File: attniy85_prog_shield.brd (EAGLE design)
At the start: 68.6 x 53.3 mm, 2 parts, among them U1 ARDUINOR3-BPLACE

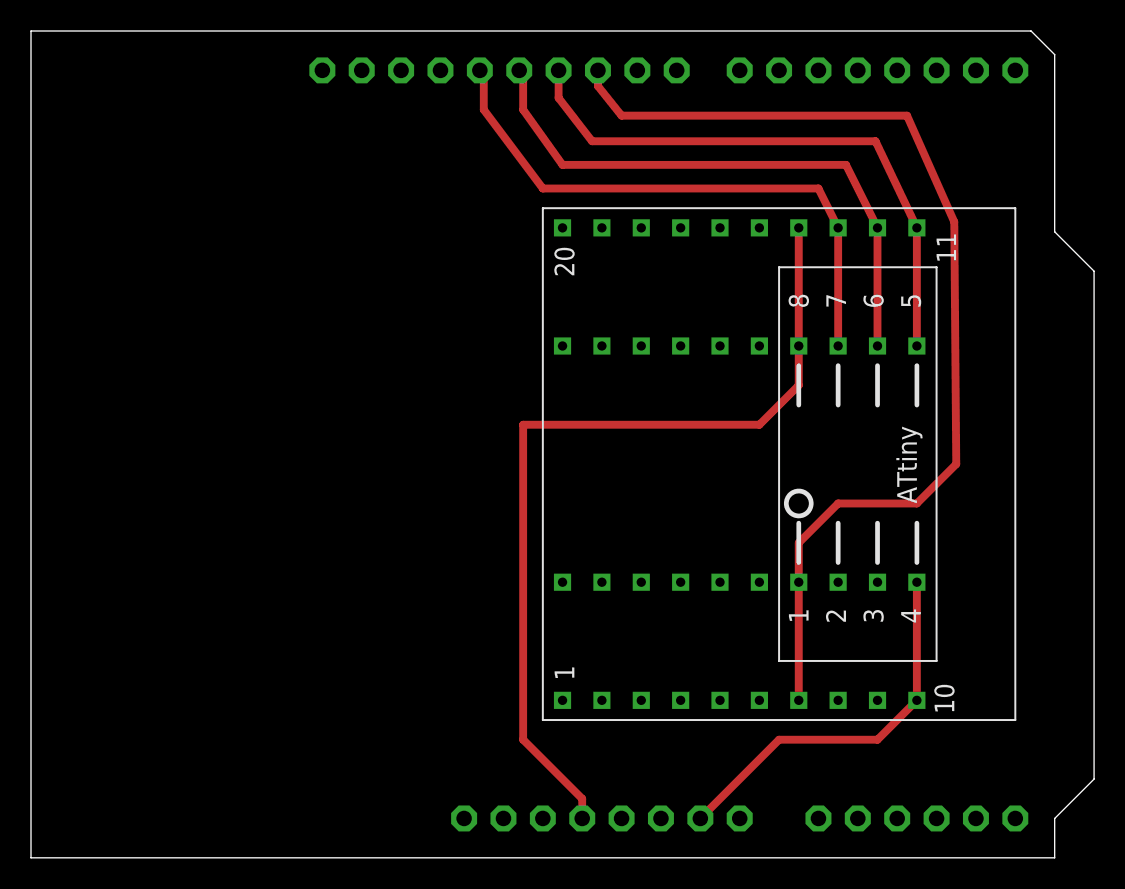
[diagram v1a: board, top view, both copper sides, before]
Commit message: unrouted 2x5pin isp
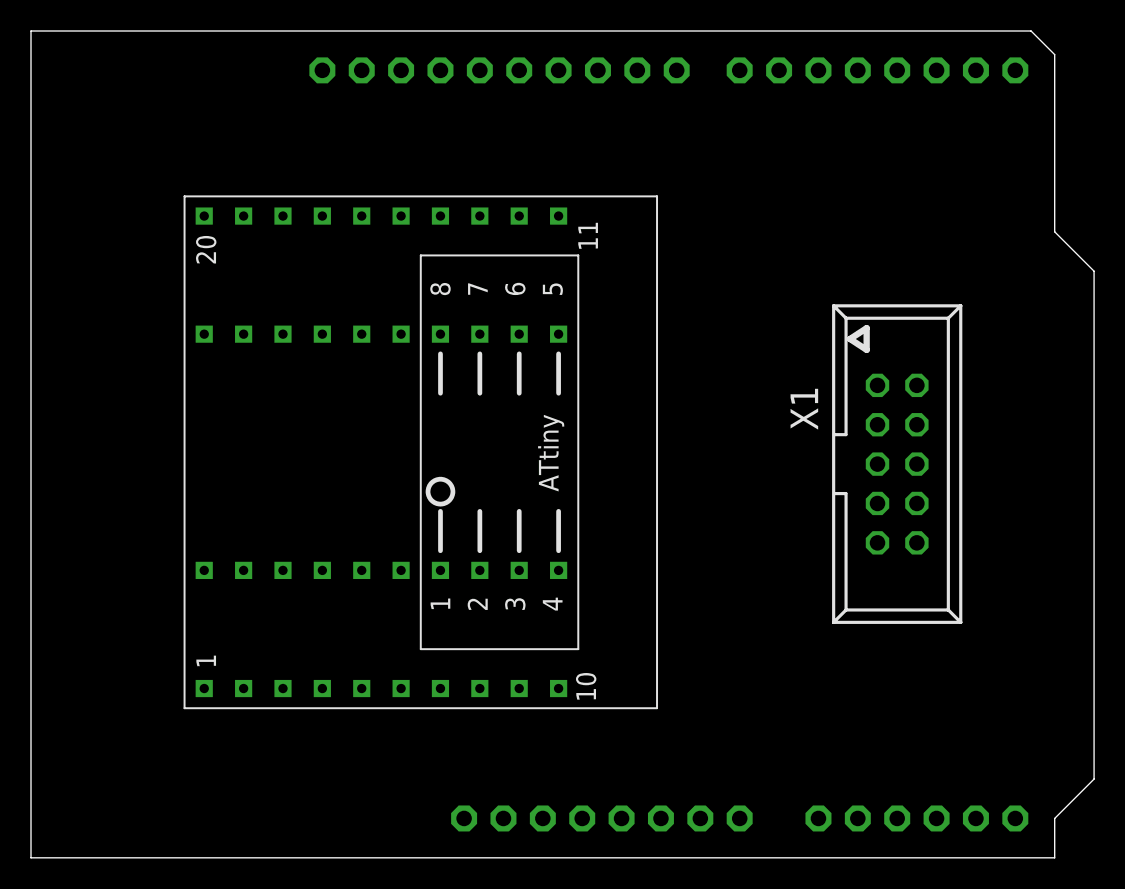
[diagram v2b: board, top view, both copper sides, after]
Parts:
- added X1: ISP10P, attniy85_prog_shield:ISP10PIN
- moved U$1 23.1 mm to (40.4, 9.65)
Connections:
- net GND: now also X1.1
- net MISO: now also X1.2
- net MOSI: now also X1.3
- net RESET: now also X1.4
- net SCK: now also X1.5
- net VCC: now also X1.6
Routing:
- net RESET: track 67.4 -> 0.00 mm
- net VCC: track 56.0 -> 0.00 mm
- net MISO: track 37.5 -> 0.00 mm
- net MOSI: track 37.4 -> 0.00 mm
- net SCK: track 37.2 -> 0.00 mm
- net GND: track 24.7 -> 0.00 mm
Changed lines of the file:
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@@
 <elements>
 <element name="U1" library="ATtami" package="ARDUINOR3-BPLACE" value="ARDUINOR3-BPLACE" x="0" y="0"/>
-<element name="U$1" library="attniy85_prog_shield" package="SOIC8-200MIL" value="SOIC8_200MIL_PROG" x="63.5" y="8.89" rot="R90"/>
+<element name="U$1" library="attniy85_prog_shield" package="SOIC8-200MIL" value="SOIC8_200MIL_PROG" x="40.386" y="9.652" rot="R90"/>
+<element name="X1" library="attniy85_prog_shield" package="ISP10PIN" value="ISP10P" x="55.88" y="25.4" rot="R270"/>
 </elements>
 <signals>
@@
 <contactref element="U1" pad="GND1"/>
 <contactref element="U$1" pad="P$10"/>
-<wire x1="43.18" y1="2.54" x2="48.26" y2="7.62" width="0.508" layer="1"/>
-<wire x1="48.26" y1="7.62" x2="54.61" y2="7.62" width="0.508" layer="1"/>
-<wire x1="54.61" y1="7.62" x2="57.15" y2="10.16" width="0.508" layer="1"/>
 <contactref element="U$1" pad="P$30"/>
-<wire x1="57.15" y1="17.78" x2="57.15" y2="10.16" width="0.508" layer="1"/>
-<wire x1="57.15" y1="17.78" x2="26.416" y2="50.8" width="0" layer="19" extent="1-1"/>
-<wire x1="40.64" y1="2.54" x2="43.18" y2="2.54" width="0" layer="19" extent="1-1"/>
+<contactref element="X1" pad="1"/>
+<wire x1="26.416" y1="50.8" x2="54.61" y2="30.48" width="0" layer="19" extent="1-1"/>
+<wire x1="40.64" y1="2.54" x2="54.61" y2="30.48" width="0" layer="19" extent="1-1"/>
+<wire x1="43.18" y1="2.54" x2="40.64" y2="2.54" width="0" layer="19" extent="1-1"/>
+<wire x1="34.036" y1="10.922" x2="43.18" y2="2.54" width="0" layer="19" extent="1-1"/>
+<wire x1="34.036" y1="18.542" x2="34.036" y2="10.922" width="0" layer="19" extent="1-1"/>
 </signal>
 <signal name="VIN">
@@
 <contactref element="U1" pad="3V"/>
 <contactref element="U$1" pad="P$34"/>
-<wire x1="49.53" y1="40.64" x2="49.53" y2="33.02" width="0.508" layer="1"/>
-<wire x1="49.53" y1="33.02" x2="49.53" y2="30.48" width="0.508" layer="1"/>
-<wire x1="49.53" y1="30.48" x2="46.99" y2="27.94" width="0.508" layer="1"/>
-<wire x1="46.99" y1="27.94" x2="31.75" y2="27.94" width="0.508" layer="1"/>
-<wire x1="31.75" y1="27.94" x2="31.75" y2="7.62" width="0.508" layer="1"/>
-<wire x1="35.56" y1="3.81" x2="35.56" y2="2.54" width="0.508" layer="1"/>
-<wire x1="31.75" y1="7.62" x2="35.56" y2="3.81" width="0.508" layer="1"/>
+<contactref element="X1" pad="6"/>
+<wire x1="26.416" y1="41.402" x2="26.416" y2="33.782" width="0" layer="19" extent="1-1"/>
+<wire x1="57.15" y1="25.4" x2="26.416" y2="33.782" width="0" layer="19" extent="1-1"/>
+<wire x1="35.56" y1="2.54" x2="57.15" y2="25.4" width="0" layer="19" extent="1-1"/>
 </signal>
 <signal name="SCK">
 <contactref element="U1" pad="D13"/>
 <contactref element="U$1" pad="P$13"/>
-<wire x1="28.956" y1="50.8" x2="29.21" y2="50.546" width="0.508" layer="1"/>
-<wire x1="29.21" y1="50.546" x2="29.21" y2="48.26" width="0.508" layer="1"/>
-<wire x1="29.21" y1="48.26" x2="33.02" y2="43.18" width="0.508" layer="1"/>
-<wire x1="33.02" y1="43.18" x2="50.8" y2="43.18" width="0.508" layer="1"/>
-<wire x1="50.8" y1="43.18" x2="52.07" y2="40.64" width="0.508" layer="1"/>
 <contactref element="U$1" pad="P$33"/>
-<wire x1="52.07" y1="40.64" x2="52.07" y2="33.02" width="0.508" layer="1"/>
+<contactref element="X1" pad="5"/>
+<wire x1="28.956" y1="33.782" x2="28.956" y2="41.402" width="0" layer="19" extent="1-1"/>
+<wire x1="28.956" y1="50.8" x2="28.956" y2="41.402" width="0" layer="19" extent="1-1"/>
+<wire x1="54.61" y1="25.4" x2="28.956" y2="50.8" width="0" layer="19" extent="1-1"/>
 </signal>
 <signal name="MISO">
 <contactref element="U1" pad="D12"/>
 <contactref element="U$1" pad="P$12"/>
-<wire x1="31.496" y1="50.8" x2="31.75" y2="50.546" width="0.508" layer="1"/>
-<wire x1="31.75" y1="50.546" x2="31.75" y2="48.26" width="0.508" layer="1"/>
-<wire x1="31.75" y1="48.26" x2="34.29" y2="44.704" width="0.508" layer="1"/>
-<wire x1="34.29" y1="44.704" x2="52.578" y2="44.704" width="0.508" layer="1"/>
-<wire x1="52.578" y1="44.704" x2="54.61" y2="40.64" width="0.508" layer="1"/>
 <contactref element="U$1" pad="P$32"/>
-<wire x1="54.61" y1="40.64" x2="54.61" y2="33.02" width="0.508" layer="1"/>
+<contactref element="X1" pad="2"/>
+<wire x1="31.496" y1="33.782" x2="31.496" y2="41.402" width="0" layer="19" extent="1-1"/>
+<wire x1="31.496" y1="50.8" x2="31.496" y2="41.402" width="0" layer="19" extent="1-1"/>
+<wire x1="57.15" y1="30.48" x2="31.496" y2="50.8" width="0" layer="19" extent="1-1"/>
 </signal>
 <signal name="MOSI">
 <contactref element="U1" pad="D11"/>
 <contactref element="U$1" pad="P$11"/>
-<wire x1="34.036" y1="50.8" x2="34.036" y2="49.022" width="0.508" layer="1"/>
-<wire x1="36.195" y1="46.228" x2="54.483" y2="46.228" width="0.508" layer="1"/>
-<wire x1="54.483" y1="46.228" x2="57.15" y2="40.64" width="0.508" layer="1"/>
-<wire x1="34.036" y1="49.022" x2="36.195" y2="46.228" width="0.508" layer="1"/>
 <contactref element="U$1" pad="P$31"/>
-<wire x1="57.15" y1="40.64" x2="57.15" y2="33.02" width="0.508" layer="1"/>
+<contactref element="X1" pad="3"/>
+<wire x1="34.036" y1="33.782" x2="34.036" y2="41.402" width="0" layer="19" extent="1-1"/>
+<wire x1="34.036" y1="50.8" x2="34.036" y2="41.402" width="0" layer="19" extent="1-1"/>
+<wire x1="54.61" y1="27.94" x2="34.036" y2="50.8" width="0" layer="19" extent="1-1"/>
 </signal>
 <signal name="RESET">
@@
 <contactref element="U$1" pad="P$7"/>
 <contactref element="U$1" pad="P$27"/>
-<wire x1="49.53" y1="17.78" x2="49.53" y2="10.16" width="0.508" layer="1"/>
-<wire x1="36.576" y1="50.8" x2="36.576" y2="49.784" width="0.508" layer="1"/>
-<wire x1="36.576" y1="49.784" x2="38.1" y2="47.879" width="0.508" layer="1"/>
-<wire x1="38.1" y1="47.879" x2="56.515" y2="47.879" width="0.508" layer="1"/>
-<wire x1="56.515" y1="47.879" x2="59.563" y2="41.021" width="0.508" layer="1"/>
-<wire x1="59.563" y1="41.021" x2="59.69" y2="25.4" width="0.508" layer="1"/>
-<wire x1="57.15" y1="22.86" x2="52.07" y2="22.86" width="0.508" layer="1"/>
-<wire x1="52.07" y1="22.86" x2="49.53" y2="20.32" width="0.508" layer="1"/>
-<wire x1="49.53" y1="20.32" x2="49.53" y2="17.78" width="0.508" layer="1"/>
-<wire x1="59.69" y1="25.4" x2="57.15" y2="22.86" width="0.508" layer="1"/>
+<contactref element="X1" pad="4"/>
+<wire x1="36.576" y1="50.8" x2="57.15" y2="27.94" width="0" layer="19" extent="1-1"/>
+<wire x1="26.416" y1="18.542" x2="57.15" y2="27.94" width="0" layer="19" extent="1-1"/>
+<wire x1="26.416" y1="10.922" x2="26.416" y2="18.542" width="0" layer="19" extent="1-1"/>
 </signal>
 <signal name="5V">
@@
 <contactref element="U$1" pad="P$8"/>
 <contactref element="U$1" pad="P$9"/>
-<wire x1="52.07" y1="10.16" x2="54.61" y2="10.16" width="0" layer="19" extent="1-1"/>
+<wire x1="28.956" y1="10.922" x2="31.496" y2="10.922" width="0" layer="19" extent="1-1"/>
 <contactref element="U$1" pad="P$29"/>
 <contactref element="U$1" pad="P$28"/>
